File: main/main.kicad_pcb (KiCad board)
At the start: 2 copper layers, 100 x 100 mm, 259 parts, among them J1 USB_C_Receptacle_USB2.0, J2 SWD, Q1 BSS138, SW1 SW_SPST, SW2 SW_SPST, SW3 SW_SPST, SW4 SW_SPST, SW5 SW_SPST, SW6 SW_SPST, U1 LN6206P332MR-G, U2 STM32F401CBUx, Y1 Crystal

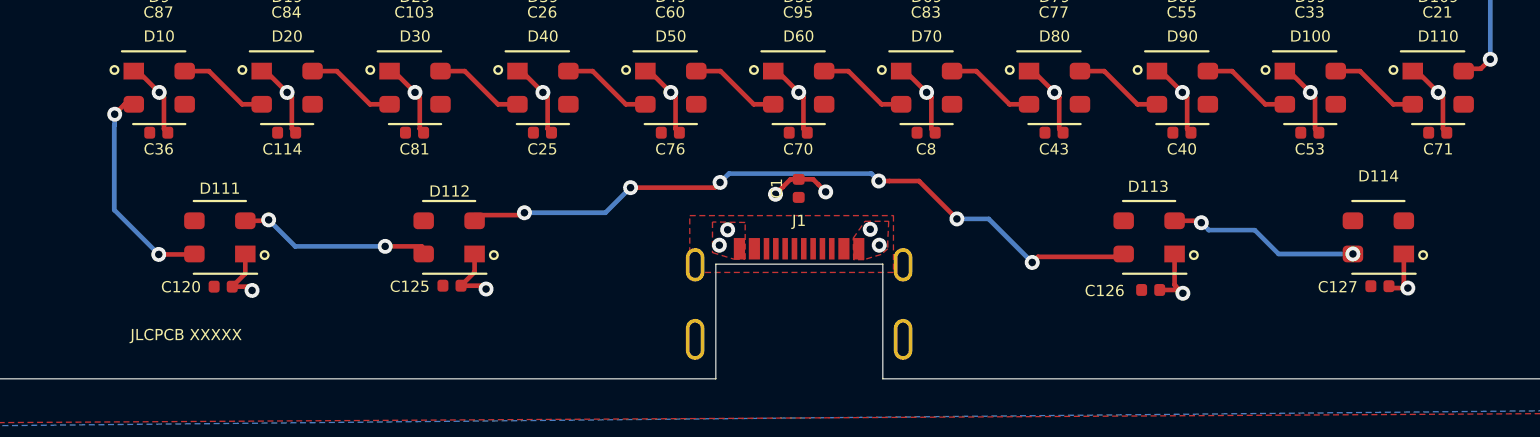
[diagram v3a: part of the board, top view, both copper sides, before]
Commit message: added front face, moved around minute mark LEDs so they were spaced evenly and as close together as possible without interfering with USB
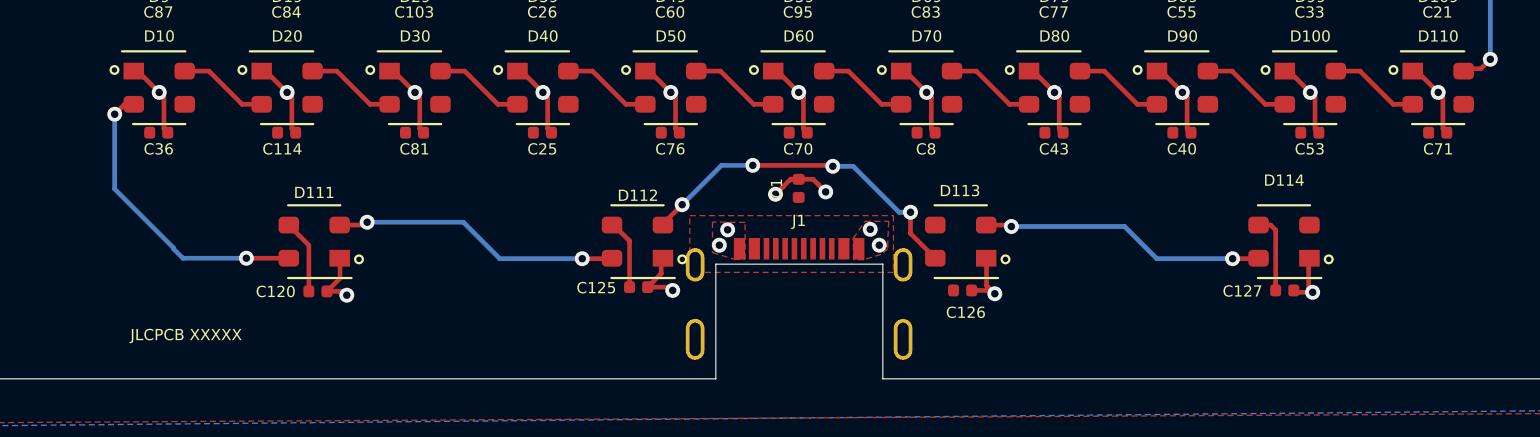
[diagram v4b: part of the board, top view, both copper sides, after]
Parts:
- moved D113 10.1 mm to (58.7, 92.6)
- moved D112 10.1 mm to (41.3, 92.6)
- moved C126 10.1 mm to (58.8, 95.3)
- moved C125 10.0 mm to (41.4, 95.1)
- moved C127 5.11 mm to (76.0, 95.3)
- moved C120 5.09 mm to (24.2, 95.3)
- moved D111 5.07 mm to (24.0, 92.6)
- moved D114 5.07 mm to (76.0, 92.6)
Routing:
- net Net-(D112-Pad2): track 37.9 -> 18.7 mm, vias 6 -> 4
- net +5V: track 5.70 -> 17.9 mm
- net Net-(D111-Pad2): track 10.2 -> 15.5 mm
- net Net-(D113-Pad2): track 10.3 -> 15.2 mm
- net Net-(D10-Pad2): track 11.7 -> 16.2 mm

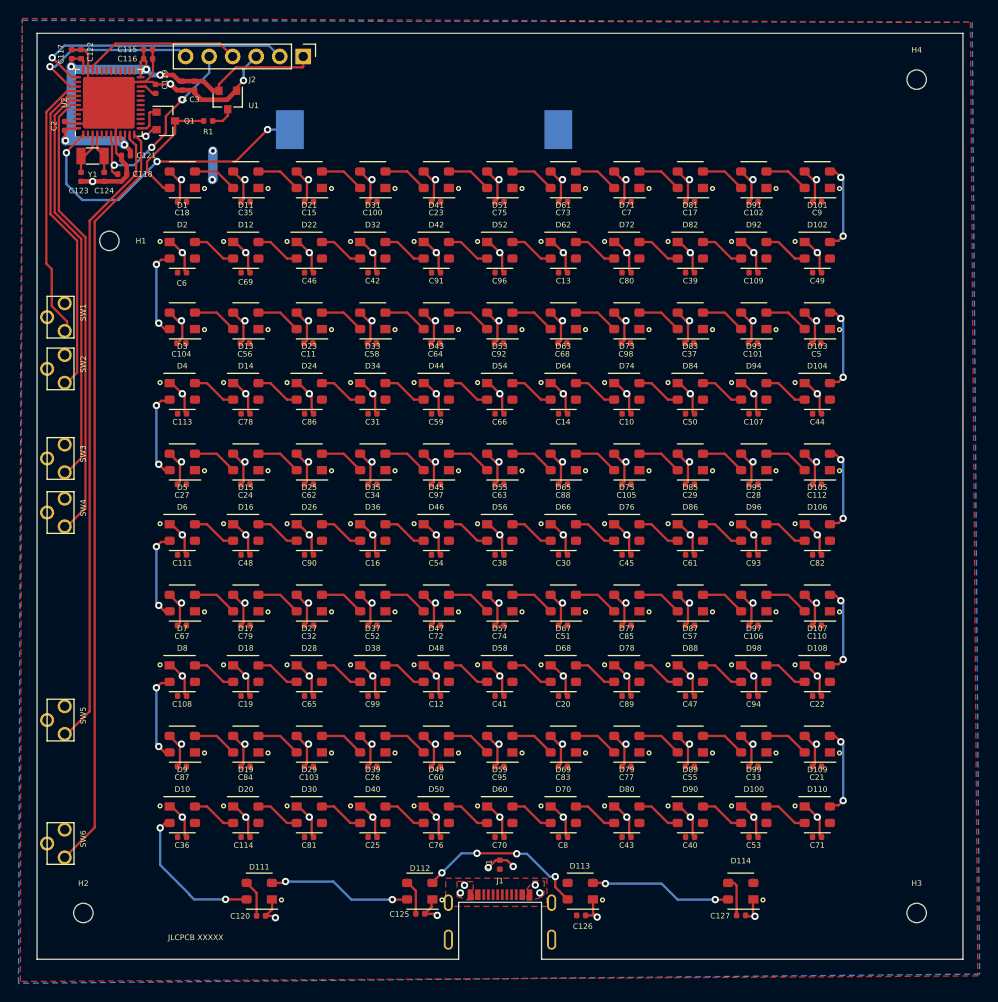
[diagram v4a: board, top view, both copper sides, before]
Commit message: progress and yet not.  trying for v0.2.0, but some issues: letters not aligned, switches to tall, minute leds too close to USB_C
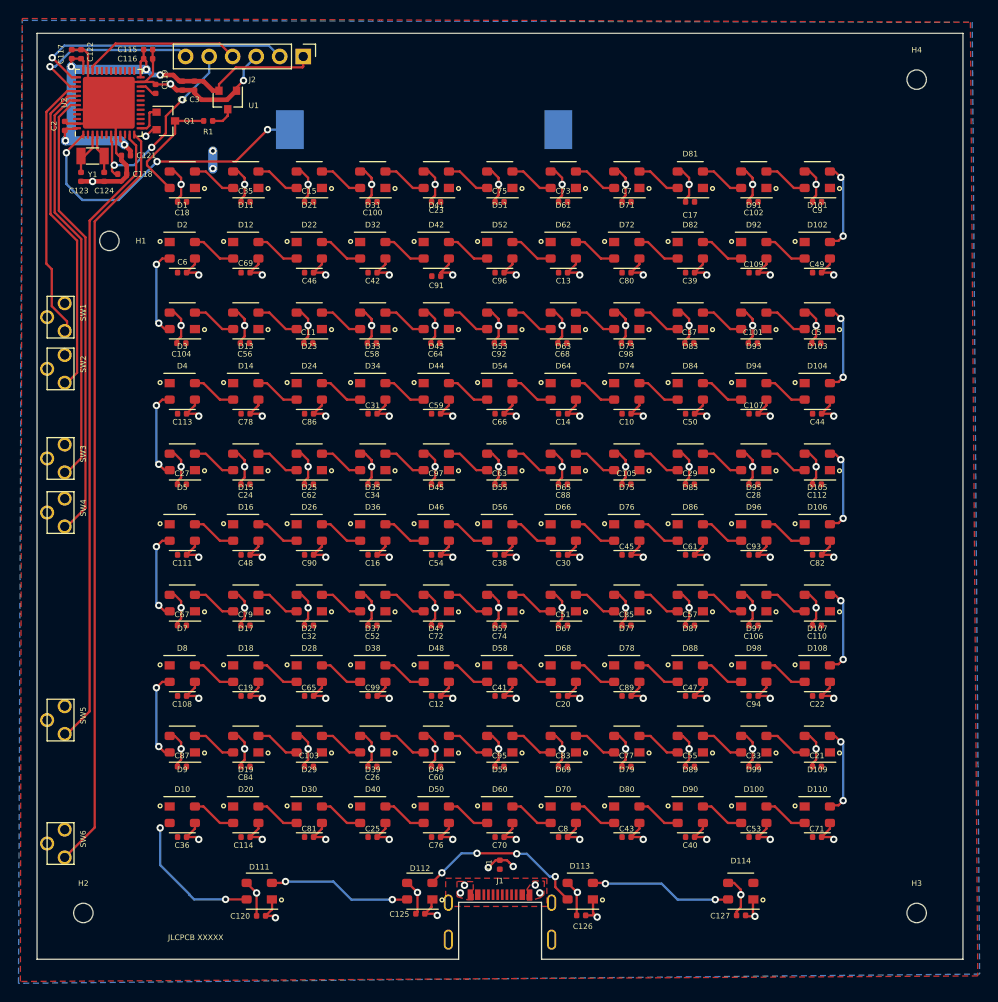
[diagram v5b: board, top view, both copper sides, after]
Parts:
- C123, C124: value 20P -> 21P
- moved C91 0.38 mm to (43.1, 26.2), turned to 180 degrees
- turned C101 to 0 degrees
- turned C103 to 0 degrees
- turned C105 to 0 degrees
- turned C107 to 180 degrees
- turned C109 to 180 degrees
- turned C11 to 0 degrees
- turned C13 to 180 degrees
- turned C15 to 0 degrees
- turned C17 to 0 degrees
- turned C19 to 180 degrees
- turned C21 to 0 degrees
- turned C23 to 0 degrees
- turned C25 to 180 degrees
- turned C27 to 0 degrees
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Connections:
- C101 pad 1: +5V -> GND
- C101 pad 2: GND -> +5V
- C103 pad 1: +5V -> GND
- C103 pad 2: GND -> +5V
- C105 pad 1: +5V -> GND
- C105 pad 2: GND -> +5V
- C107 pad 1: +5V -> GND
- C107 pad 2: GND -> +5V
- C109 pad 1: +5V -> GND
- C109 pad 2: GND -> +5V
- C11 pad 1: +5V -> GND
- C11 pad 2: GND -> +5V
- C120 pad 1: +5V -> GND
- C120 pad 2: GND -> +5V
- C125 pad 1: +5V -> GND
- C125 pad 2: GND -> +5V
- C126 pad 1: +5V -> GND
- C126 pad 2: GND -> +5V
- C127 pad 1: +5V -> GND
- C127 pad 2: GND -> +5V
- C13 pad 1: +5V -> GND
- C13 pad 2: GND -> +5V
- C15 pad 1: +5V -> GND
- C15 pad 2: GND -> +5V
- C17 pad 1: +5V -> GND
- C17 pad 2: GND -> +5V
- C19 pad 1: +5V -> GND
- C19 pad 2: GND -> +5V
- C21 pad 1: +5V -> GND
- C21 pad 2: GND -> +5V
- C23 pad 1: +5V -> GND
- C23 pad 2: GND -> +5V
- C25 pad 1: +5V -> GND
- C25 pad 2: GND -> +5V
- C27 pad 1: +5V -> GND
- C27 pad 2: GND -> +5V
- C29 pad 1: +5V -> GND
- C29 pad 2: GND -> +5V
- C31 pad 1: +5V -> GND
- C31 pad 2: GND -> +5V
- C33 pad 1: +5V -> GND
- C33 pad 2: GND -> +5V
- C35 pad 1: +5V -> GND
- C35 pad 2: GND -> +5V
- C37 pad 1: +5V -> GND
- C37 pad 2: GND -> +5V
- C39 pad 1: +5V -> GND
- C39 pad 2: GND -> +5V
- C41 pad 1: +5V -> GND
- C41 pad 2: GND -> +5V
- C43 pad 1: +5V -> GND
- C43 pad 2: GND -> +5V
- C45 pad 1: +5V -> GND
- C45 pad 2: GND -> +5V
- C47 pad 1: +5V -> GND
- C47 pad 2: GND -> +5V
- C49 pad 1: +5V -> GND
- C49 pad 2: GND -> +5V
- C5 pad 1: +5V -> GND
- C5 pad 2: GND -> +5V
- C51 pad 1: +5V -> GND
- C51 pad 2: GND -> +5V
- C53 pad 1: +5V -> GND
- C53 pad 2: GND -> +5V
- C55 pad 1: +5V -> GND
- C55 pad 2: GND -> +5V
- C57 pad 1: +5V -> GND
- C57 pad 2: GND -> +5V
- C59 pad 1: +5V -> GND
- C59 pad 2: GND -> +5V
- C6 pad 1: +5V -> GND
- C6 pad 2: GND -> +5V
- C61 pad 1: +5V -> GND
- C61 pad 2: GND -> +5V
- C63 pad 1: +5V -> GND
- C63 pad 2: GND -> +5V
- C65 pad 1: +5V -> GND
- C65 pad 2: GND -> +5V
- C67 pad 1: +5V -> GND
- C67 pad 2: GND -> +5V
- C69 pad 1: +5V -> GND
- C69 pad 2: GND -> +5V
- C7 pad 1: +5V -> GND
- C7 pad 2: GND -> +5V
- C71 pad 1: +5V -> GND
- C71 pad 2: GND -> +5V
- C73 pad 1: +5V -> GND
- C73 pad 2: GND -> +5V
- C75 pad 1: +5V -> GND
- C75 pad 2: GND -> +5V
- C77 pad 1: +5V -> GND
- C77 pad 2: GND -> +5V
- C79 pad 1: +5V -> GND
- C79 pad 2: GND -> +5V
- C8 pad 1: +5V -> GND
- C8 pad 2: GND -> +5V
- C81 pad 1: +5V -> GND
- C81 pad 2: GND -> +5V
- C83 pad 1: +5V -> GND
- C83 pad 2: GND -> +5V
- C85 pad 1: +5V -> GND
- C85 pad 2: GND -> +5V
- C87 pad 1: +5V -> GND
- C87 pad 2: GND -> +5V
- C89 pad 1: +5V -> GND
- C89 pad 2: GND -> +5V
- C9 pad 1: +5V -> GND
- C9 pad 2: GND -> +5V
- C91 pad 1: +5V -> GND
- C91 pad 2: GND -> +5V
- C93 pad 1: +5V -> GND
- C93 pad 2: GND -> +5V
- C95 pad 1: +5V -> GND
- C95 pad 2: GND -> +5V
- C97 pad 1: +5V -> GND
- C97 pad 2: GND -> +5V
- C99 pad 1: +5V -> GND
- C99 pad 2: GND -> +5V
- D10 pad 1: GND -> +5V
- D10 pad 3: +5V -> GND
- D100 pad 1: GND -> +5V
- D100 pad 3: +5V -> GND
- D102 pad 1: GND -> +5V
- D102 pad 3: +5V -> GND
- D104 pad 1: GND -> +5V
- D104 pad 3: +5V -> GND
- D106 pad 1: GND -> +5V
- D106 pad 3: +5V -> GND
- D108 pad 1: GND -> +5V
- D108 pad 3: +5V -> GND
- D110 pad 1: GND -> +5V
- D110 pad 3: +5V -> GND
- D111 pad 1: GND -> +5V
- D111 pad 3: +5V -> GND
- D112 pad 1: GND -> +5V
- D112 pad 3: +5V -> GND
- D113 pad 1: GND -> +5V
- D113 pad 3: +5V -> GND
- D114 pad 1: GND -> +5V
- D114 pad 2: /LEDs/DOUT -> (no net)
- D114 pad 3: +5V -> GND
- D12 pad 1: GND -> +5V
- D12 pad 3: +5V -> GND
- D14 pad 1: GND -> +5V
- D14 pad 3: +5V -> GND
- D16 pad 1: GND -> +5V
- D16 pad 3: +5V -> GND
- D18 pad 1: GND -> +5V
- D18 pad 3: +5V -> GND
- D2 pad 1: GND -> +5V
- D2 pad 3: +5V -> GND
- D20 pad 1: GND -> +5V
- D20 pad 3: +5V -> GND
- D22 pad 1: GND -> +5V
- D22 pad 3: +5V -> GND
- D24 pad 1: GND -> +5V
- D24 pad 3: +5V -> GND
- D26 pad 1: GND -> +5V
- D26 pad 3: +5V -> GND
- D28 pad 1: GND -> +5V
- D28 pad 3: +5V -> GND
- D30 pad 1: GND -> +5V
- D30 pad 3: +5V -> GND
- D32 pad 1: GND -> +5V
- D32 pad 3: +5V -> GND
- D34 pad 1: GND -> +5V
- D34 pad 3: +5V -> GND
- D36 pad 1: GND -> +5V
- D36 pad 3: +5V -> GND
- D38 pad 1: GND -> +5V
- D38 pad 3: +5V -> GND
- D4 pad 1: GND -> +5V
- D4 pad 3: +5V -> GND
- D40 pad 1: GND -> +5V
- D40 pad 3: +5V -> GND
- D42 pad 1: GND -> +5V
- D42 pad 3: +5V -> GND
- D44 pad 1: GND -> +5V
- D44 pad 3: +5V -> GND
- D46 pad 1: GND -> +5V
- D46 pad 3: +5V -> GND
- D48 pad 1: GND -> +5V
- D48 pad 3: +5V -> GND
- D50 pad 1: GND -> +5V
- D50 pad 3: +5V -> GND
- D52 pad 1: GND -> +5V
- D52 pad 3: +5V -> GND
- D54 pad 1: GND -> +5V
- D54 pad 3: +5V -> GND
- D56 pad 1: GND -> +5V
- D56 pad 3: +5V -> GND
- D58 pad 1: GND -> +5V
- D58 pad 3: +5V -> GND
- D6 pad 1: GND -> +5V
- D6 pad 3: +5V -> GND
- D60 pad 1: GND -> +5V
- D60 pad 3: +5V -> GND
- D62 pad 1: GND -> +5V
- D62 pad 3: +5V -> GND
- D64 pad 1: GND -> +5V
- D64 pad 3: +5V -> GND
- D66 pad 1: GND -> +5V
- D66 pad 3: +5V -> GND
- D68 pad 1: GND -> +5V
- D68 pad 3: +5V -> GND
- D70 pad 1: GND -> +5V
- D70 pad 3: +5V -> GND
- D72 pad 1: GND -> +5V
- D72 pad 3: +5V -> GND
- D74 pad 1: GND -> +5V
- D74 pad 3: +5V -> GND
- D76 pad 1: GND -> +5V
- D76 pad 3: +5V -> GND
- D78 pad 1: GND -> +5V
- D78 pad 3: +5V -> GND
- D8 pad 1: GND -> +5V
- D8 pad 3: +5V -> GND
- D80 pad 1: GND -> +5V
- D80 pad 3: +5V -> GND
- D82 pad 1: GND -> +5V
- D82 pad 3: +5V -> GND
- D84 pad 1: GND -> +5V
- D84 pad 3: +5V -> GND
- D86 pad 1: GND -> +5V
- D86 pad 3: +5V -> GND
- D88 pad 1: GND -> +5V
- D88 pad 3: +5V -> GND
- D90 pad 1: GND -> +5V
- D90 pad 3: +5V -> GND
- D92 pad 1: GND -> +5V
- D92 pad 3: +5V -> GND
- D94 pad 1: GND -> +5V
- D94 pad 3: +5V -> GND
- D96 pad 1: GND -> +5V
- D96 pad 3: +5V -> GND
- D98 pad 1: GND -> +5V
- D98 pad 3: +5V -> GND
- J1 pad A5: Net-(J1-PadA5) -> (no net)
- J1 pad A6: Net-(J1-PadA6) -> (no net)
- J1 pad A7: Net-(J1-PadA7) -> (no net)
- J1 pad A8: Net-(J1-PadA8) -> (no net)
- J1 pad B5: Net-(J1-PadB5) -> (no net)
- J1 pad B6: Net-(J1-PadB6) -> (no net)
- J1 pad B7: Net-(J1-PadB7) -> (no net)
- J1 pad B8: Net-(J1-PadB8) -> (no net)
- U2 pad 10: Net-(U2-Pad10) -> (no net)
- U2 pad 14: Net-(U2-Pad14) -> (no net)
- U2 pad 15: Net-(U2-Pad15) -> (no net)
- U2 pad 16: Net-(U2-Pad16) -> (no net)
- U2 pad 17: Net-(U2-Pad17) -> (no net)
- U2 pad 18: Net-(U2-Pad18) -> (no net)
- U2 pad 19: Net-(U2-Pad19) -> (no net)
- U2 pad 2: Net-(U2-Pad2) -> (no net)
- U2 pad 20: Net-(U2-Pad20) -> (no net)
- U2 pad 21: Net-(U2-Pad21) -> (no net)
- U2 pad 25: Net-(U2-Pad25) -> (no net)
- U2 pad 26: Net-(U2-Pad26) -> (no net)
- U2 pad 27: Net-(U2-Pad27) -> (no net)
- U2 pad 28: Net-(U2-Pad28) -> (no net)
- U2 pad 29: Net-(U2-Pad29) -> (no net)
- U2 pad 30: Net-(U2-Pad30) -> (no net)
- U2 pad 31: Net-(U2-Pad31) -> (no net)
- U2 pad 32: Net-(U2-Pad32) -> (no net)
- U2 pad 33: Net-(U2-Pad33) -> (no net)
- U2 pad 38: Net-(U2-Pad38) -> (no net)
- U2 pad 45: Net-(U2-Pad45) -> (no net)
- U2 pad 46: Net-(U2-Pad46) -> (no net)
- U2 pad 5: Net-(U2-Pad5) -> (no net)
- U2 pad 6: Net-(U2-Pad6) -> (no net)
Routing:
- net GND: track 537.4 -> 496.3 mm
- net Net-(D10-Pad2): track 16.2 -> 14.9 mm
- net Net-(D109-Pad2): track 9.59 -> 8.87 mm
- net Net-(D107-Pad2): track 9.59 -> 8.87 mm
- net Net-(D105-Pad2): track 9.59 -> 8.87 mm
- net Net-(D103-Pad2): track 9.59 -> 8.87 mm
- net Net-(D101-Pad2): track 9.59 -> 8.87 mm
- net Net-(D6-Pad2): track 9.59 -> 9.05 mm
- net Net-(D4-Pad2): track 9.59 -> 9.05 mm
- net Net-(D2-Pad2): track 9.59 -> 9.05 mm
- net Net-(D8-Pad2): track 9.59 -> 9.05 mm
- net +5V: track 17.9 -> 17.7 mm, vias 2 -> 6
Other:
- board text added: "BRIGHT (HOLD)"
- board text added: "WORD CLOCK v0.2.0 batch 0 12/12/2019"
- board text removed: "BRIGHTNESS (HOLD)"
- board text removed: "WORD CLOCK v0.1.0 batch 0 12/11/2019"
